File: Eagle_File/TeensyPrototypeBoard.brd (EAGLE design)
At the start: 58.3 x 51.7 mm, 50 parts, among them Q1 16mhz, SW1 SPST_TACT-KMR2, SW2 SPST_TACT-KMR2, U3 BLE112-A, X1 32.768khz

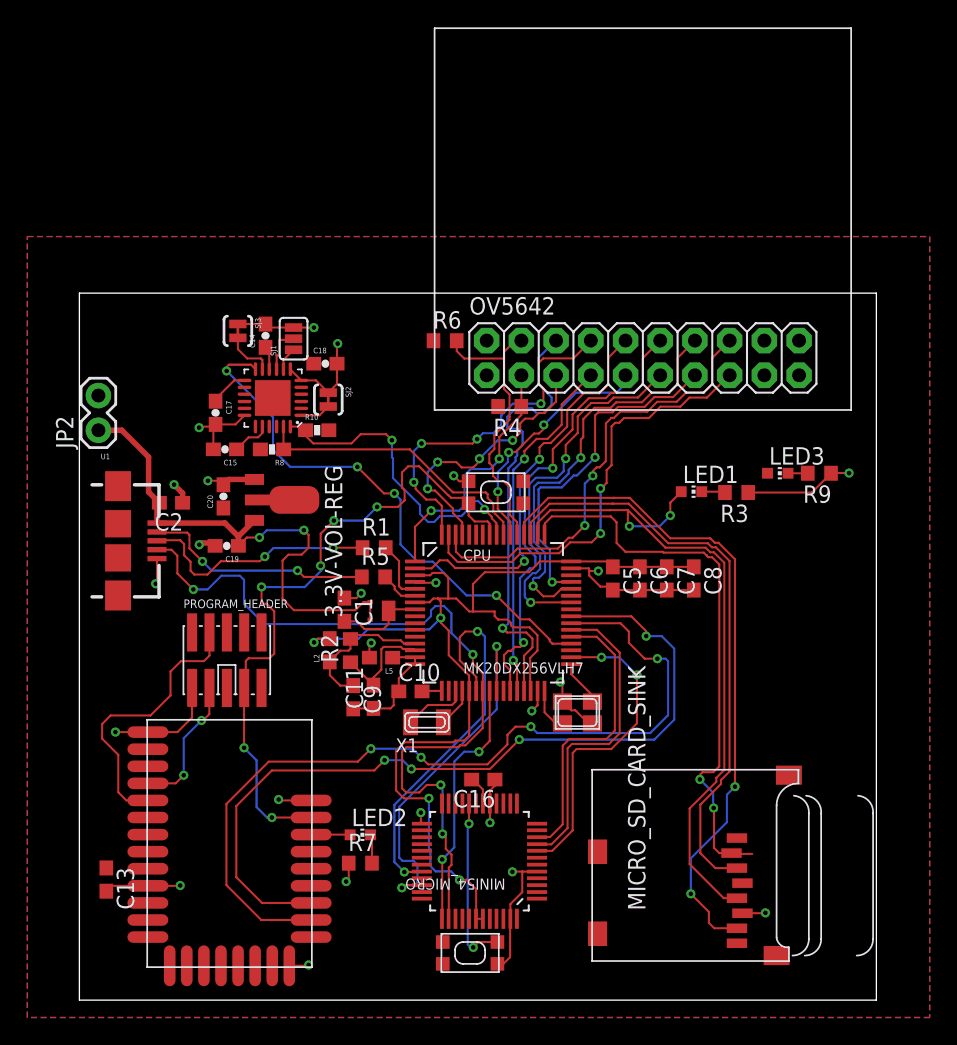
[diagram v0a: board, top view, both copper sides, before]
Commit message: modify the name and value on the board
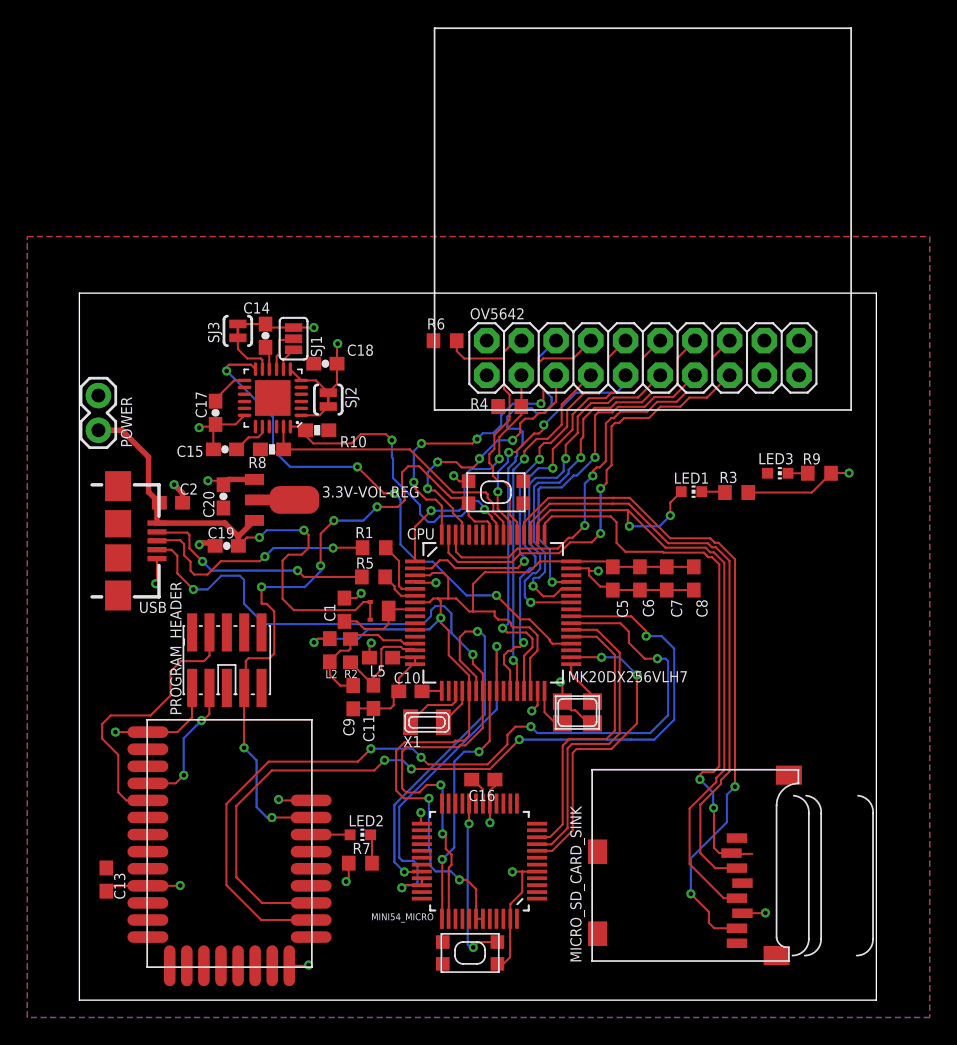
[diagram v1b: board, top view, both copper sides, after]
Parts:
- renumbered JP2 to POWER, U1 to USB
